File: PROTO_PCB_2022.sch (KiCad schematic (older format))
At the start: 14 parts, among them J1 ECU_EN_CONNECTION, K1 RT214012, K2 RT214012

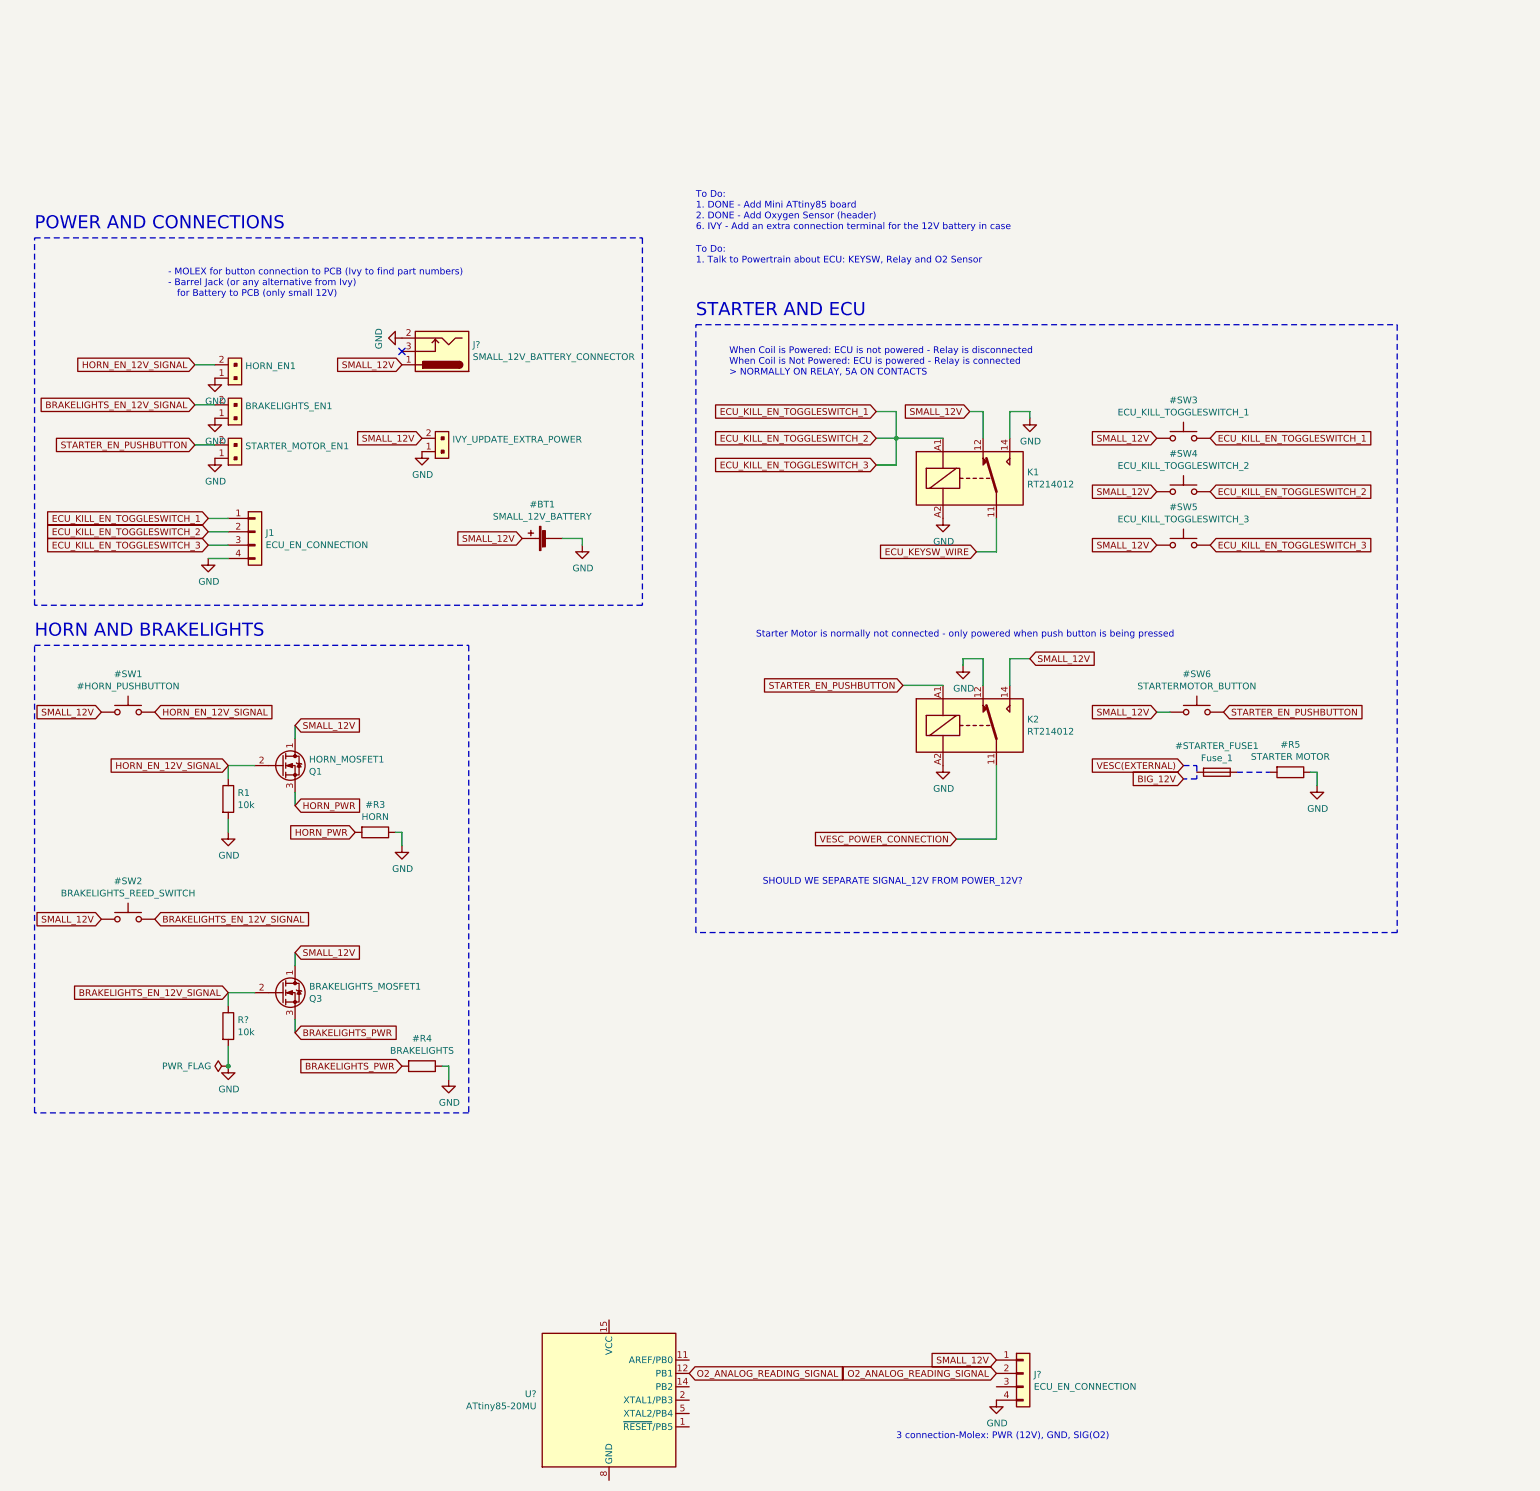
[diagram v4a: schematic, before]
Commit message: Review and fix power connectors
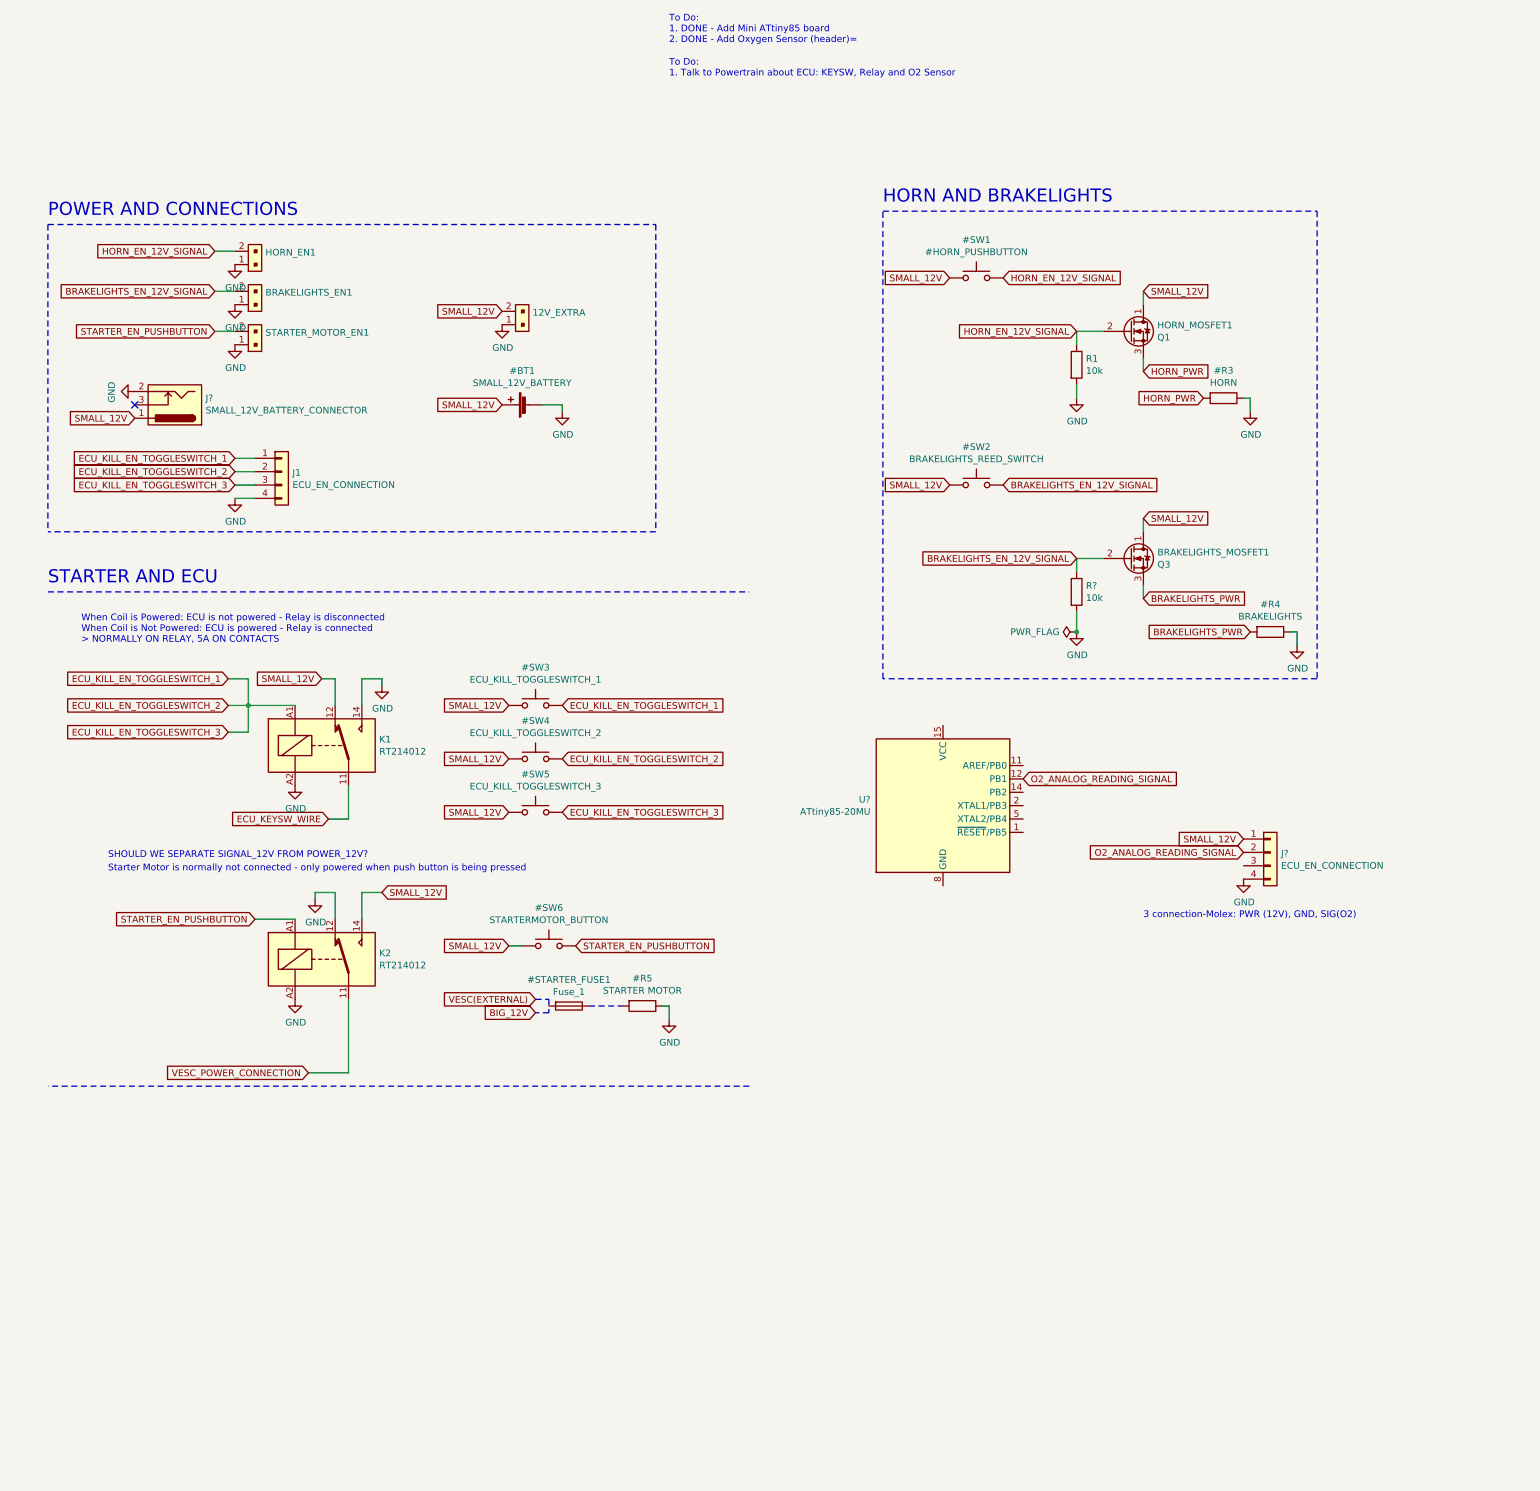
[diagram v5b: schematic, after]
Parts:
- renumbered IVY_UPDATE_EXTRA_POWER to 12V_EXTRA
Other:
- note added: "To Do:\n1. DONE - Add Mini ATtiny85 board\n2. DONE - Add Oxygen Sensor (header)="
- note removed: "- MOLEX for button connection to PCB (Ivy to find part numbers)\n- Barrel Jack (or any alternative from Ivy) \n for Battery to PCB (only small 12V)"
- note removed: "To Do:\n1. DONE - Add Mini ATtiny85 board\n2. DONE - Add Oxygen Sensor (header)\n6. IVY - Add an extra connection terminal for the 12V battery in case"
- moved on the sheet: 12V_EXTRA, BRAKELIGHTS_EN1, BRAKELIGHTS_MOSFET1, HORN_EN1, HORN_MOSFET1, J1, J?, K1, K2, R1, R?, STARTER_MOTOR_EN1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

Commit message: Added O2 sensor connector
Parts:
- J?: footprint Connector_Molex:Molex_CLIK-Mate_505405-0470_1x04-1MP_P1.50mm_Vertical -> Connector_Molex:Molex_Micro-Fit_3.0_43650-0315_1x03_P3.00mm_Vertical; symbol Connector_Generic:Conn_01x04 -> Connector_Generic:Conn_01x03; DigikeyPN (none) -> WM1918-ND; MPN (none) -> 0436500315
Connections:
- net GND: now also J?.3 (Pin_3); no longer J?.4 (Pin_4)
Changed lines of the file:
@@
 3 connection-Molex: PWR (12V), GND, SIG(O2)
 $Comp
-L Connector_Generic:Conn_01x04 J?
+L Connector_Generic:Conn_01x03 J?
 U 1 1 61E82140
 P 10050 5700
 F 0 "J?" H 10130 5692 50  0000 L CNN
 F 1 "ECU_EN_CONNECTION" H 10130 5601 50  0000 L CNN
-F 2 "Connector_Molex:Molex_CLIK-Mate_505405-0470_1x04-1MP_P1.50mm_Vertical" H 10050 5700 50  0001 C CNN
-F 3 "~" H 10050 5700 50  0001 C CNN
+F 2 "Connector_Molex:Molex_Micro-Fit_3.0_43650-0315_1x03_P3.00mm_Vertical" H 10050 5700 50  0001 C CNN
+F 3 "https://www.molex.com/pdm_docs/sd/436500315_sd.pdf" H 10050 5700 50  0001 C CNN
+F 4 "WM1918-ND" H 10050 5700 50  0001 C CNN "DigikeyPN"
+F 5 "0436500315" H 10050 5700 50  0001 C CNN "MPN"
 	1    10050 5700
 	1    0    0    -1
@@
 L power:GND #PWR?
 U 1 1 61E84B3F
-P 9850 5900
-F 0 "#PWR?" H 9850 5650 50  0001 C CNN
-F 1 "GND" H 9855 5727 50  0000 C CNN
-F 2 "" H 9850 5900 50  0001 C CNN
-F 3 "" H 9850 5900 50  0001 C CNN
-	1    9850 5900
+P 9850 5800
+F 0 "#PWR?" H 9850 5550 50  0001 C CNN
+F 1 "GND" H 9855 5627 50  0000 C CNN
+F 2 "" H 9850 5800 50  0001 C CNN
+F 3 "" H 9850 5800 50  0001 C CNN
+	1    9850 5800
 	1    0    0    -1
 $EndComp

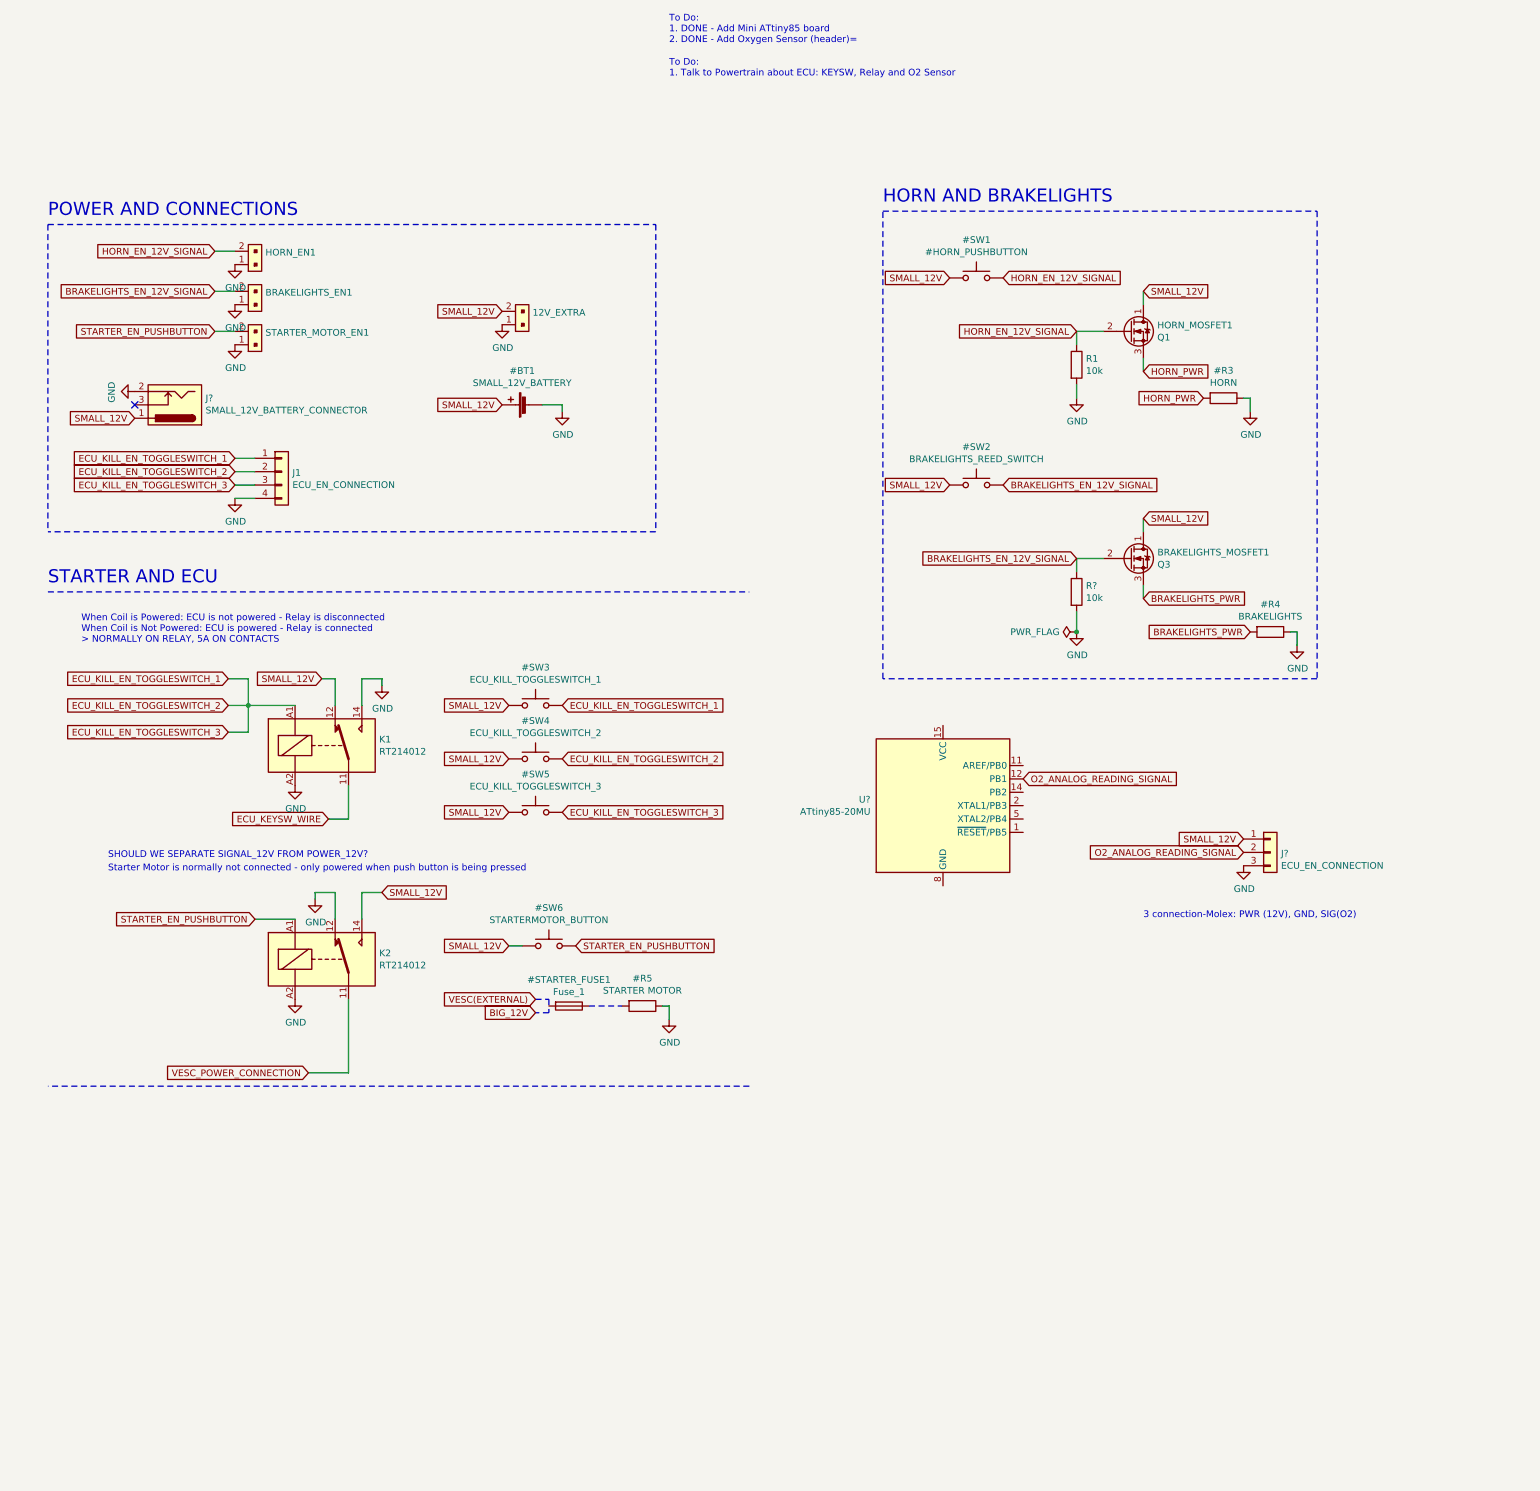
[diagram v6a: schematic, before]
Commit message: Changed power connectors to terminal blocks, updated molex connectors
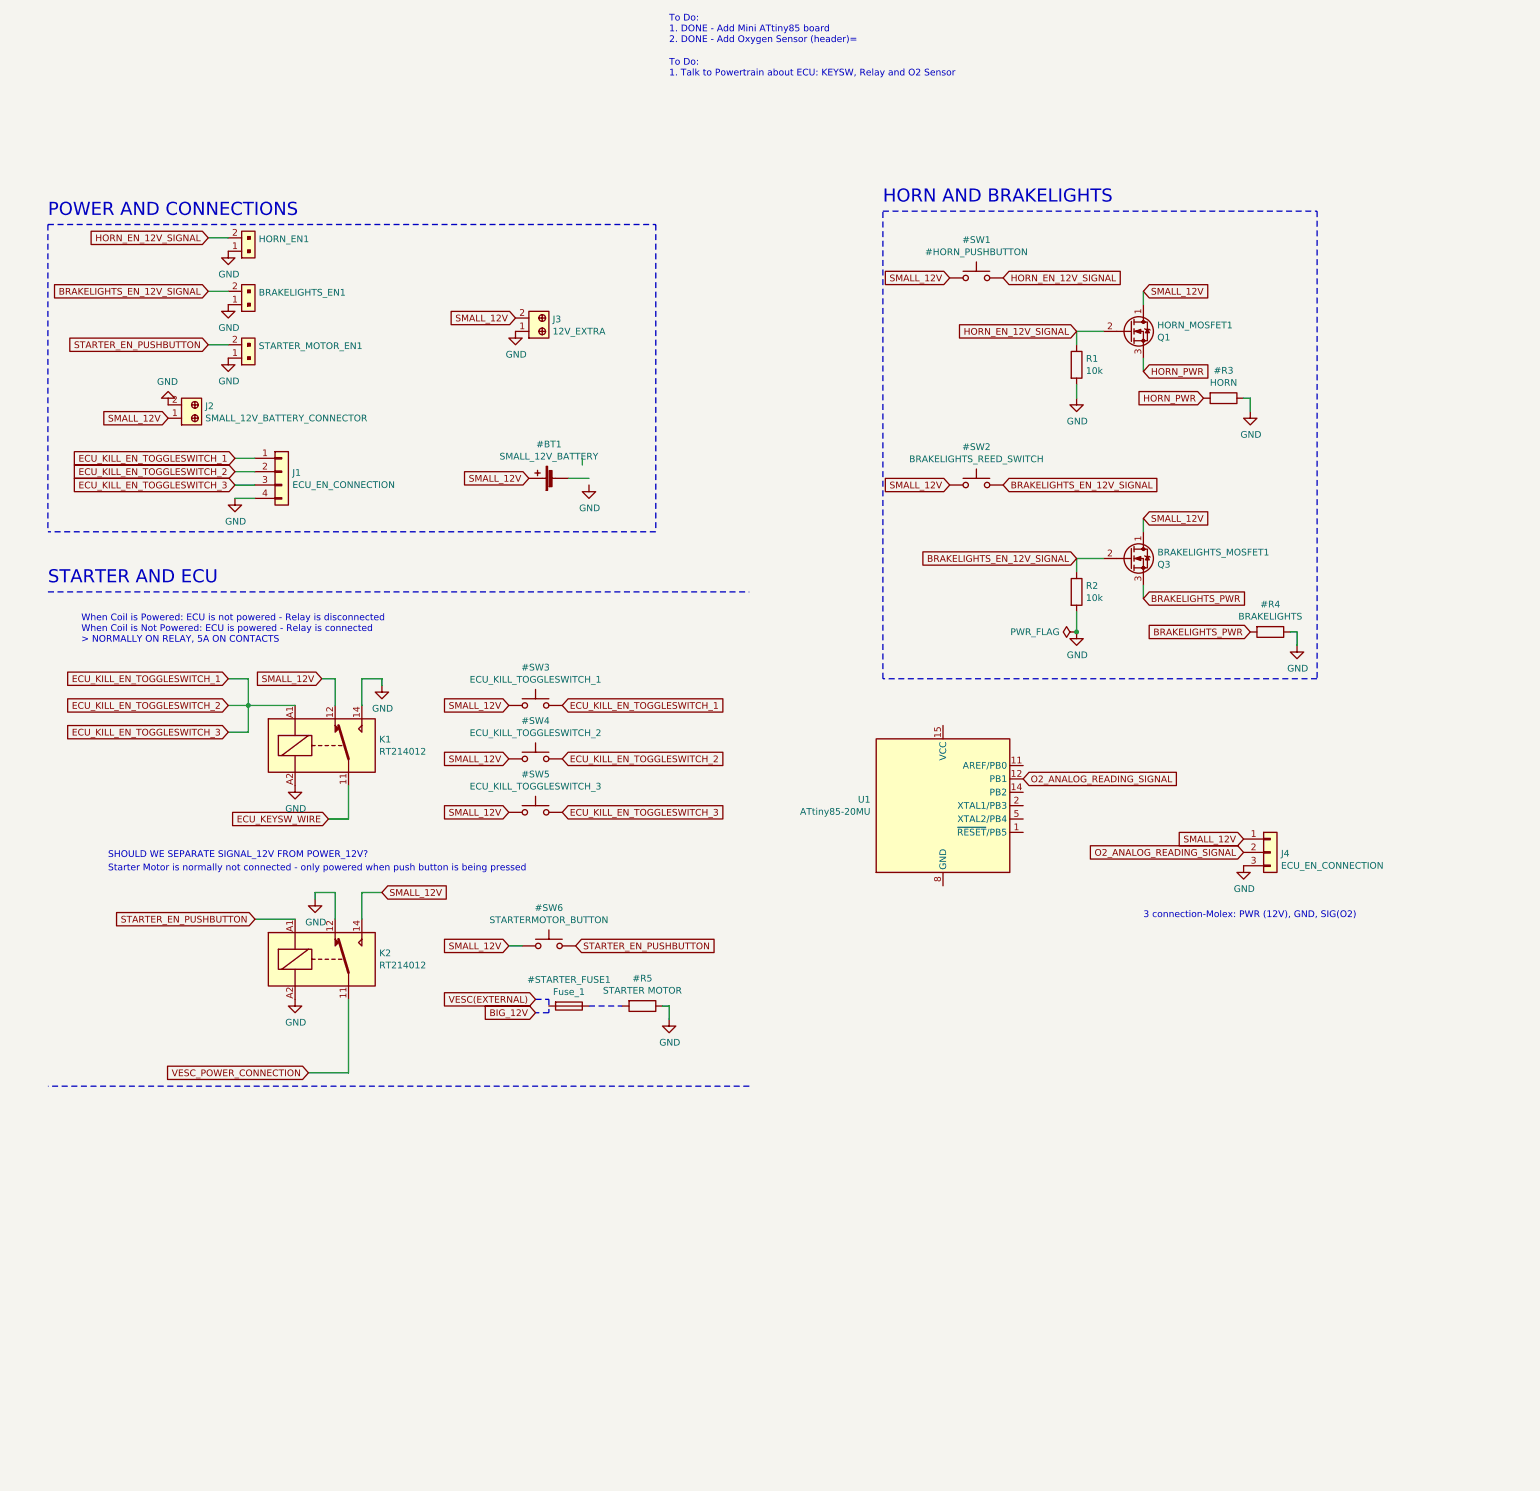
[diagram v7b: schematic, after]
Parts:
- removed 12V_EXTRA: Conn_?, symbol PROTO_PCB_2022-rescue:B2B-PH-K-S_LF__SN_-dk_Rectangular-Connectors-Headers-Male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
- removed J?: SMALL_12V_BATTERY_CONNECTOR, Connector_BarrelJack:BarrelJack_CUI_PJ-036AH-SMT_Horizontal, symbol Connector:Barrel_Jack_Switch
- added J2: SMALL_12V_BATTERY_CONNECTOR, digikey-footprints:Terminal_Block_D1.3mm_P5mm, symbol dk_Terminal-Blocks-Wire-to-Board:1935161
- added J3: 12V_EXTRA, digikey-footprints:Terminal_Block_D1.3mm_P5mm, symbol dk_Terminal-Blocks-Wire-to-Board:1935161
- BRAKELIGHTS_EN1, HORN_EN1, STARTER_MOTOR_EN1: footprint Connector_Molex:Molex_CLIK-Mate_502386-0270_1x02-1MP_P1.25mm_Horizontal -> Connector_Molex:Molex_Micro-Fit_3.0_43045-0218_2x01-1MP_P3.00mm_Vertical; DigiKeyPN WM4946CT-ND -> WM1801CT-ND; MPN 5023860270 -> 0430450218
- gave numbers to parts that had none: 3
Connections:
- no-connect marks 1 -> 0
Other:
- moved on the sheet: BRAKELIGHTS_EN1, HORN_EN1, STARTER_MOTOR_EN1
